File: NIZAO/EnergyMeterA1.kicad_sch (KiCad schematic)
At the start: 27 parts, among them U12 BL0942, U13 B0303S-1WR3_C7465185, U14 ISO7021DR

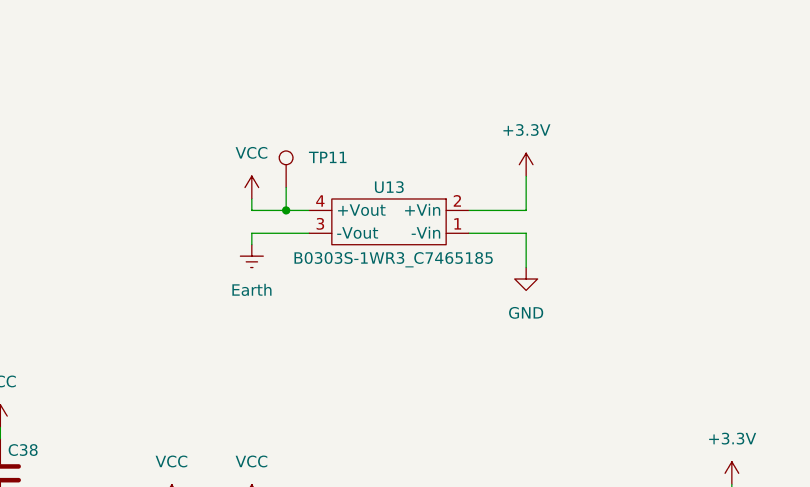
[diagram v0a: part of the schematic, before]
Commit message: Colocandos los 3d de los componetes en la placa NIZAO
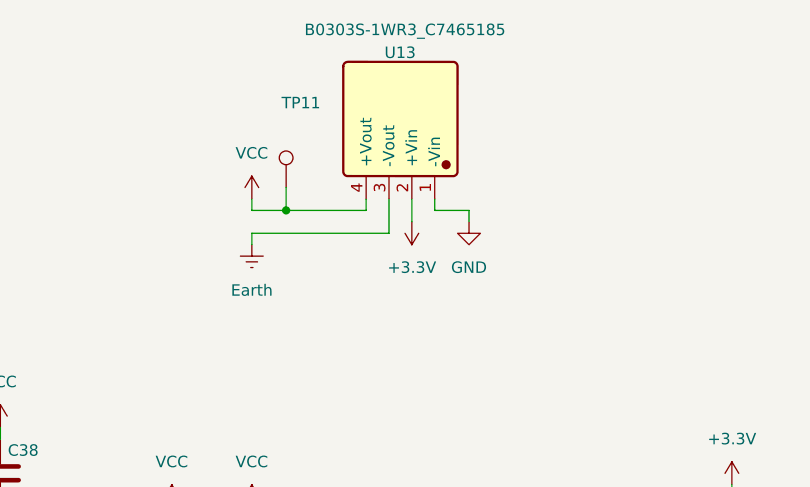
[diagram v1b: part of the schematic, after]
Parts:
- U12: footprint BL BL0942:SSOP-10_L4.9-W3.9-P1.00-LS6.0-BL -> JLCImport:BL0942
- U13: footprint EVISUN B0303S-1WR3:PWRM-TH_BXXXXS-1WR3 -> JLCImport:B0303S-1WR3_C7465185; symbol EasyEDA:B0303S-1WR3_C7465185 -> JLCImport:B0303S-1WR3_C7465185; LCSC (none) -> C7465185; Manufacturer (none) -> EVISUN; Manufacturer Part (none) -> B0303S-1WR3
- U14: footprint TI ISO7021DR:SOIC-8_L4.9-W3.9-P1.27-LS6.0-BL -> JLCImport:ISO7021DR
